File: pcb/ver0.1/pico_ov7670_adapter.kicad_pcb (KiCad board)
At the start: 2 copper layers, 45 x 54 mm, 21 parts, among them J1 GPIO Header, SW1 SW_Push, SW2 SW_Push, U1 CAMERA-OV7670, U2 RASPBERRY_PI_PICO_W

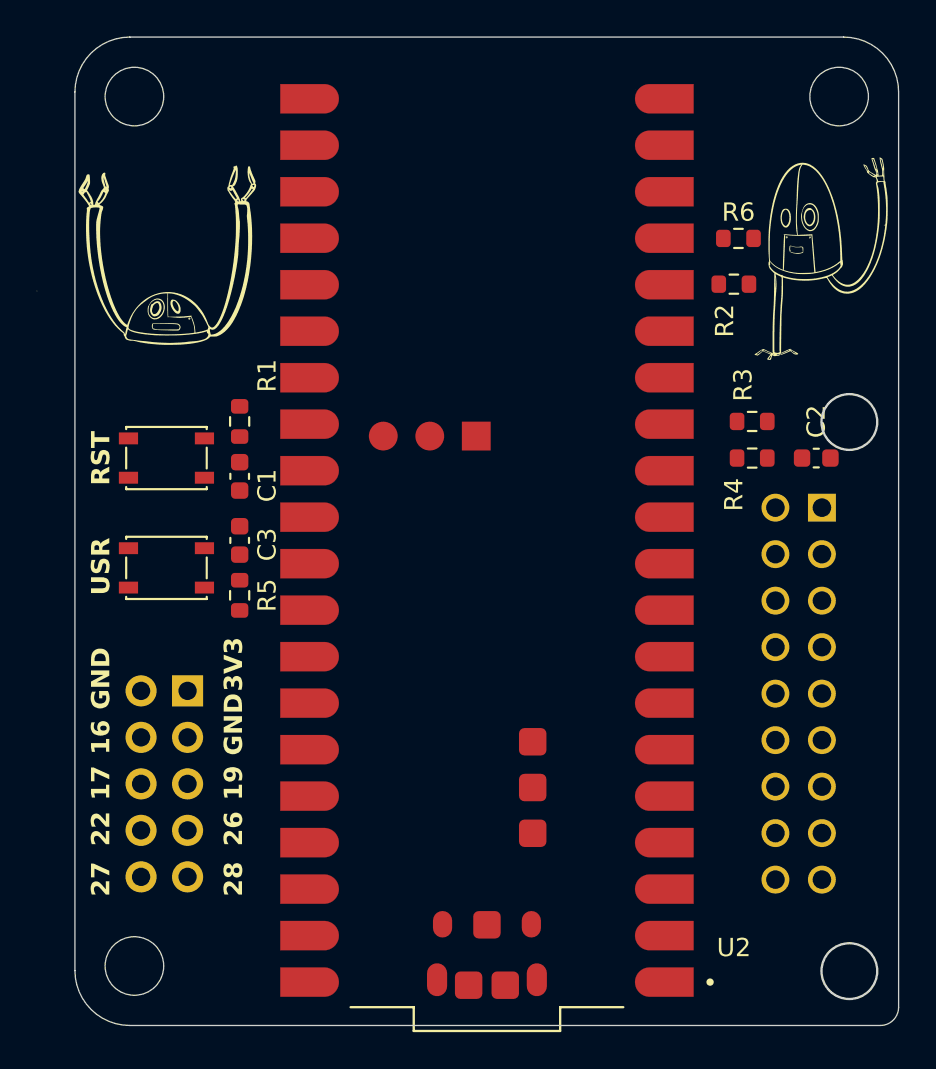
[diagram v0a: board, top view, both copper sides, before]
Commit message: layout updated as per the feedback.
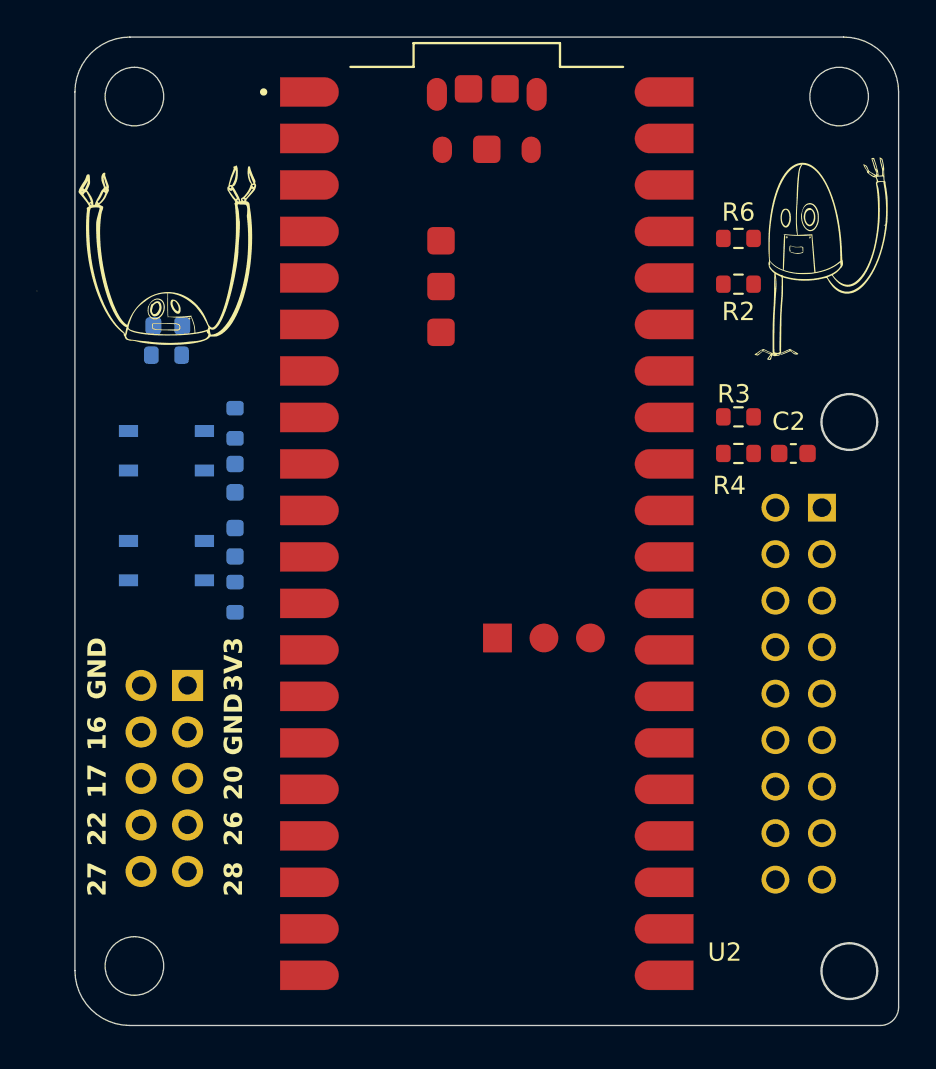
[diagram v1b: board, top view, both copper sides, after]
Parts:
- added D1: USER LED, LED_SMD:LED_0603_1608Metric, B.Cu at (95.1, 81.8)
- added R7: 1K, Resistor_SMD:R_0603_1608Metric, B.Cu at (95.0, 83.4)
- C1, C3, R1, R5, SW1, SW2: moved to B.Cu
- moved G*** 32.6 mm to (128.2, 77.4)
- moved R1 9.60 mm to (98.8, 96.6), turned to 90 degrees
- moved R5 9.40 mm to (98.8, 87.1), turned to 90 degrees
- moved SW2 6.40 mm to (95.0, 88.6)
- moved SW1 5.60 mm to (95.0, 94.6)
- moved C1 3.61 mm to (98.8, 93.6), turned to 90 degrees
- moved C3 3.41 mm to (98.8, 90.1), turned to -90 degrees
- moved C2 1.27 mm to (129.2, 88.8)
- moved G*** 1.01 mm to (113.3, 75.6)
- moved R3 0.79 mm to (126.2, 86.8)
- moved R4 0.79 mm to (126.2, 88.8)
- moved U2 0.37 mm to (112.5, 93.1), turned to 0 degrees
- moved J1 0.30 mm to (96.2, 101.4)
- moved R2 0.25 mm to (126.2, 79.5)
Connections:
- J1 pad 5: /PICO_IO19 -> /PICO_IO20
- U2 pad 25: /PICO_IO19 -> /USER_LED
- U2 pad 26: unconnected-(U2-I2C0_SDA/GP20-Pad26) -> /PICO_IO20
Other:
- board text added: "20"
- board text added: "PICO 2 OV7670 Adapter"
- board text added: "Ver 0.1"
- board text removed: "19"
- board text removed: "PICO 2 OV7670 Adapter 0.1"

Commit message: basic rotuing completed
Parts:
- U2: value RASPBERRY_PI_PICO_W -> MODULE_RASPBERRY_PI_PICO_W
- moved R2 12.1 mm to (125.2, 91.6), turned to 90 degrees
- moved R6 10.9 mm to (125.2, 87.8), turned to 90 degrees
- moved R4 8.37 mm to (129.4, 81.0), turned to -90 degrees
- moved R3 5.86 mm to (127.4, 81.0), turned to -90 degrees
- moved R1 3.35 mm to (98.8, 93.2), turned to -90 degrees
- moved C1 2.65 mm to (98.8, 96.2), turned to -90 degrees
- moved C2 1.57 mm to (128.0, 87.8), turned to 90 degrees
- moved H2 1.00 mm to (93.2, 70.2)
- moved H3 1.00 mm to (131.8, 70.2)
- moved G*** 0.72 mm to (113.4, 76.3)
- moved G*** 0.63 mm to (128.0, 78.0)
- moved G*** 0.35 mm to (129.8, 79.0)
- moved SW1 0.15 mm to (95.0, 94.8)
- moved D1 0.08 mm to (95.0, 81.8)
- turned R5 to -90 degrees
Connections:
- net OV_PCLK_PICO_IO9 renamed OV_PCLK_PICO_IO4
- net OV_XCLK_PICO_IO8 renamed OV_XCLK_PICO_IO5
- J1 pad 10: /PICO_IO27 -> /PICO_IO16
- J1 pad 4: /PICO_IO16 -> /PICO_IO22
- J1 pad 5: /PICO_IO20 -> /PICO_IO21
- J1 pad 6: /PICO_IO17 -> /PICO_IO20
- J1 pad 7: /PICO_IO26 -> /PICO_IO19
- J1 pad 8: /PICO_IO22 -> /PICO_IO18
- J1 pad 9: /PICO_IO28 -> /PICO_IO17
- R2 pad 2: Net-(U2-UART0_TX/I2C0_SDA/SPI1_RX/GP12) -> Net-(U2-UART1_RX/I2C0_SCL/SPI0_CSN/GP5)
- R3 pad 2: OV_SCL_PICO_IO13_SCL -> OV_SCL_PICO_IO1_SCL
- R4 pad 2: OV_SDA_PICO_IO12_SDA -> OV_SDA_PICO_IO0_SDA
- R6 pad 2: Net-(U2-UART0_RX/I2C0_SCL/SPI1_CSN/GP13) -> Net-(U2-UART1_TX/I2C0_SDA/SPI0_RX/GP4)
- U1 pad 11: OV_SDA_PICO_IO12_SDA -> OV_SDA_PICO_IO0_SDA
- U1 pad 12: OV_HREF_PICO_IO11 -> OV_HREF_PICO_IO3
- U1 pad 14: OV_D6_PICO_IO6 -> OV_D6_PICO_IO7
- U1 pad 15: OV_D4_PICO_IO4 -> OV_D4_PICO_IO9
- U1 pad 16: OV_D2_PICO_IO2 -> OV_D2_PICO_IO12
- U1 pad 17: OV_D0_PICO_IO0 -> OV_D0_PICO_IO14
- U1 pad 2: OV_D1_PICO_IO1 -> OV_D1_PICO_IO13
- U1 pad 3: OV_D3_PICO_IO3 -> OV_D3_PICO_IO10
- U1 pad 4: OV_D5_PICO_IO5 -> OV_D5_PICO_IO8
- U1 pad 5: OV_D7_PICO_IO7 -> OV_D7_PICO_IO6
- U1 pad 7: OV_VSYNC_PICO_IO10 -> OV_VSYNC_PICO_IO2
- U1 pad 8: OV_SCL_PICO_IO13_SCL -> OV_SCL_PICO_IO1_SCL
- U2 pad 1: OV_D0_PICO_IO0 -> OV_SDA_PICO_IO0_SDA
- U2 pad 10: OV_D7_PICO_IO7 -> OV_D6_PICO_IO7
- U2 pad 11: OV_SDA_PICO_IO12_SDA -> OV_D5_PICO_IO8
- U2 pad 12: OV_SCL_PICO_IO13_SCL -> OV_D4_PICO_IO9
- U2 pad 14: OV_HREF_PICO_IO11 -> OV_D3_PICO_IO10
- U2 pad 15: OV_VSYNC_PICO_IO10 -> OV_D2_PICO_IO12
- U2 pad 16: Net-(U2-UART0_TX/I2C0_SDA/SPI1_RX/GP12) -> OV_D1_PICO_IO13
- U2 pad 17: Net-(U2-UART0_RX/I2C0_SCL/SPI1_CSN/GP13) -> OV_D0_PICO_IO14
- U2 pad 2: OV_D1_PICO_IO1 -> OV_SCL_PICO_IO1_SCL
- U2 pad 24: /USER_Button -> /PICO_IO18
- U2 pad 25: /USER_LED -> /PICO_IO19
- U2 pad 27: unconnected-(U2-12C0_SCL/GP21-Pad27) -> /PICO_IO21
- U2 pad 31: /PICO_IO26 -> /USER_Button
- U2 pad 32: /PICO_IO27 -> unconnected-(U2-I2C1_SCL/ADC1/GP27-Pad32)
- U2 pad 34: /PICO_IO28 -> /USER_LED
- U2 pad 4: OV_D2_PICO_IO2 -> OV_VSYNC_PICO_IO2
- U2 pad 5: OV_D3_PICO_IO3 -> OV_HREF_PICO_IO3
- U2 pad 6: OV_D4_PICO_IO4 -> Net-(U2-UART1_TX/I2C0_SDA/SPI0_RX/GP4)
- U2 pad 7: OV_D5_PICO_IO5 -> Net-(U2-UART1_RX/I2C0_SCL/SPI0_CSN/GP5)
- U2 pad 9: OV_D6_PICO_IO6 -> OV_D7_PICO_IO6
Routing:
- net +3V3: track 0.00 -> 87.3 mm, vias 0 -> 5
- net OV_SDA_PICO_IO0_SDA: track 0.00 -> 59.8 mm
- net OV_SCL_PICO_IO1_SCL: track 0.00 -> 45.4 mm
- net OV_VSYNC_PICO_IO2: track 0.00 -> 42.3 mm
- net /PICO_IO22: track 0.00 -> 40.2 mm
- net OV_HREF_PICO_IO3: track 0.00 -> 38.6 mm
- net OV_D7_PICO_IO6: track 0.00 -> 35.6 mm
- net /PICO_RESET: track 0.00 -> 35.4 mm, vias 0 -> 1
- net OV_D5_PICO_IO8: track 0.00 -> 33.5 mm
- net /USER_Button: track 0.00 -> 32.6 mm, vias 0 -> 1
- net /USER_LED: track 0.00 -> 32.3 mm, vias 0 -> 1
- net /PICO_IO16: track 0.00 -> 32.2 mm
- net OV_D6_PICO_IO7: track 0.00 -> 31.6 mm
- net /PICO_IO20: track 0.00 -> 31.6 mm
- net /PICO_IO18: track 0.00 -> 30.3 mm
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- added copper zone on B.Cu, net GND
- added copper zone on F.Cu, net GND
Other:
- board size 45 x 54 mm -> 45 x 53 mm
- board text added: "18"
- board text added: "19"
- board text added: "21"
- board text removed: "26"
- board text removed: "27"
- board text removed: "28"

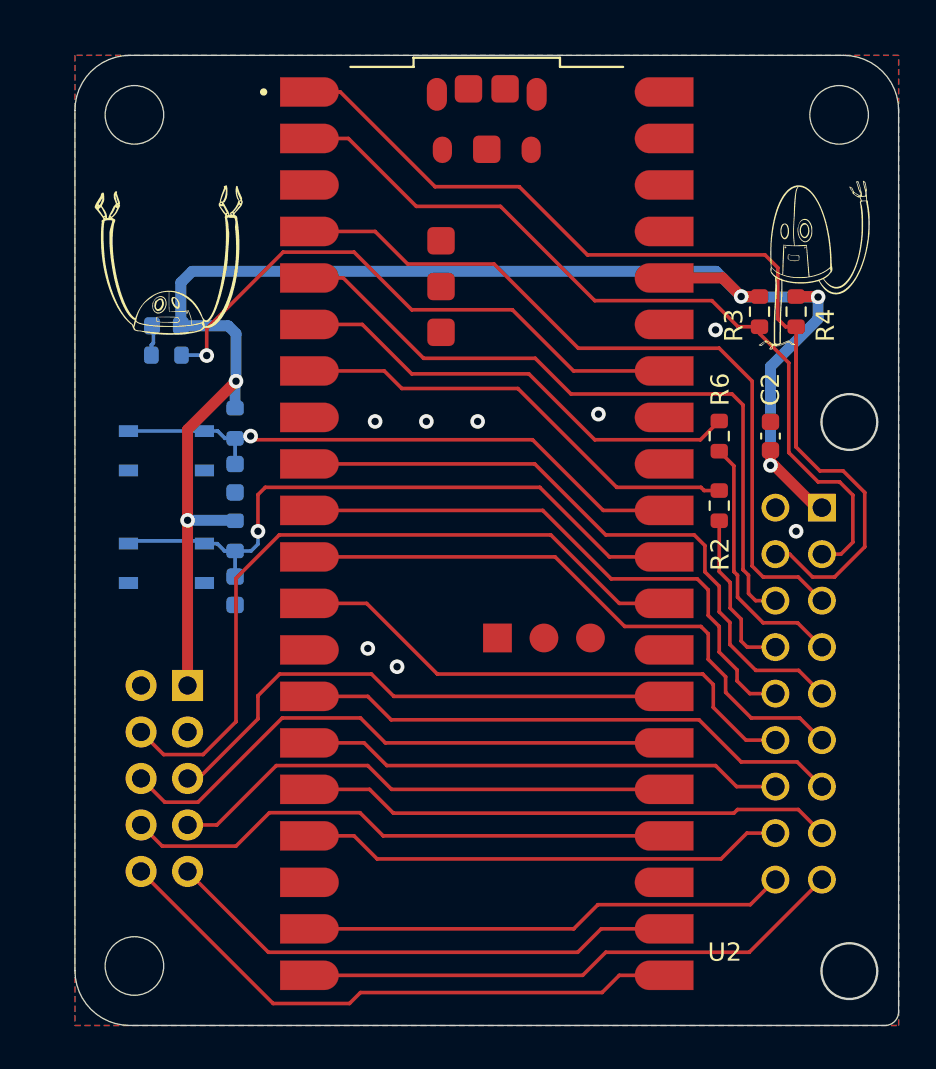
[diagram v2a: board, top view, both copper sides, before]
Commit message: GPIO header change updated
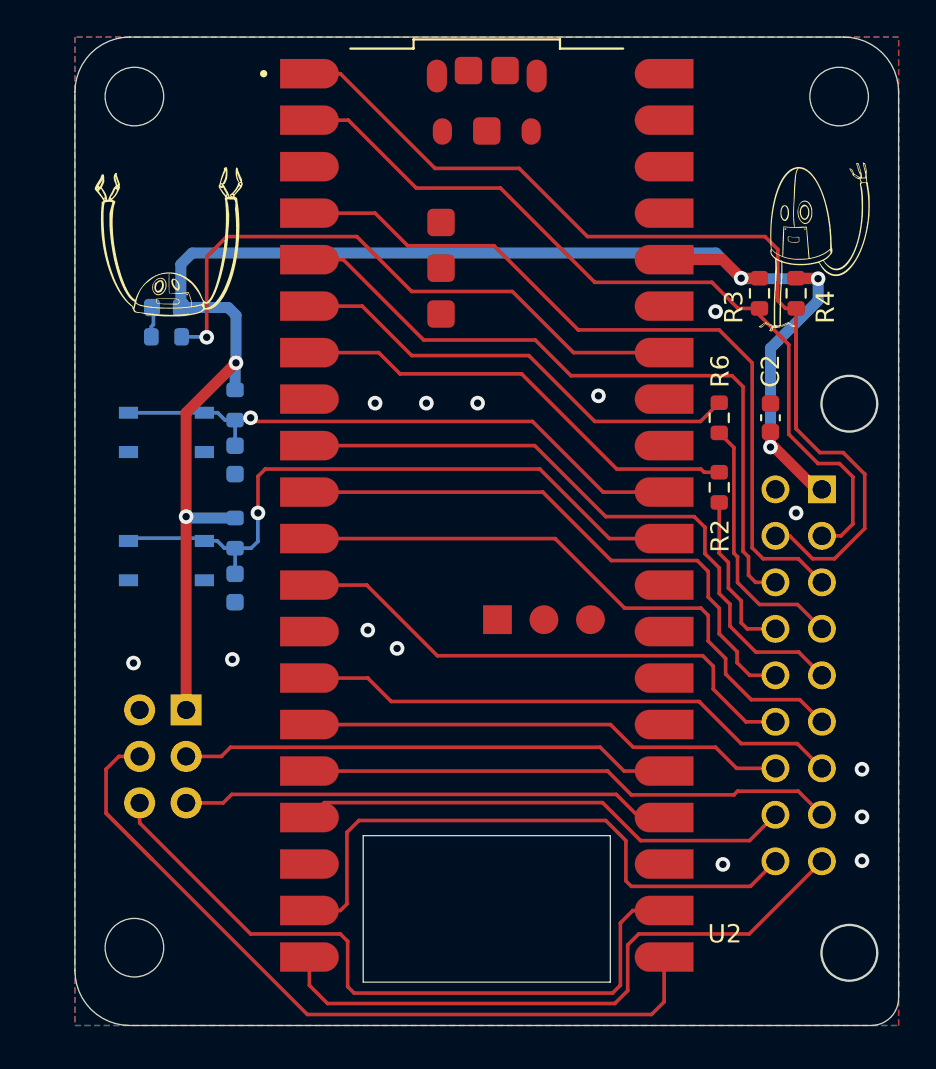
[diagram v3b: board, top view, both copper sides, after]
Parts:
- J1: footprint Connector_PinHeader_2.54mm:PinHeader_2x05_P2.54mm_Vertical -> Connector_PinHeader_2.54mm:PinHeader_2x03_P2.54mm_Vertical
- moved J1 1.34 mm to (96.1, 102.8)
- moved C2 1.00 mm to (128.0, 86.8)
- moved C3 1.00 mm to (98.8, 89.1)
- moved D1 1.00 mm to (95.0, 80.8)
- moved G*** 1.00 mm to (95.5, 78.5)
- moved G*** 1.00 mm to (129.8, 78.0)
- moved G*** 1.00 mm to (113.4, 75.3)
- moved G*** 1.00 mm to (128.0, 77.0)
- moved H1 1.00 mm to (93.2, 115.8)
- moved H2 1.00 mm to (93.2, 69.2)
- moved H3 1.00 mm to (131.8, 69.2)
- moved R2 1.00 mm to (125.2, 90.6)
- moved R3 1.00 mm to (127.4, 80.0)
- moved R4 1.00 mm to (129.4, 80.0)
- moved R5 1.00 mm to (98.8, 86.1)
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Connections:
- J1 pad 3: GND -> /PICO_IO19
- J1 pad 4: /PICO_IO22 -> /PICO_IO16
- J1 pad 5: /PICO_IO21 -> /PICO_IO18
- J1 pad 6: /PICO_IO20 -> /PICO_IO17
- U2 pad 26: /PICO_IO20 -> unconnected-(U2-I2C0_SDA/GP20-Pad26)
- U2 pad 27: /PICO_IO21 -> unconnected-(U2-12C0_SCL/GP21-Pad27)
- U2 pad 29: /PICO_IO22 -> unconnected-(U2-GP22-Pad29)
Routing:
- net /PICO_IO22: track 40.2 -> 0.00 mm
- net /PICO_IO20: track 31.6 -> 0.00 mm
- net /PICO_IO21: track 29.7 -> 0.00 mm
- net /PICO_IO16: track 32.2 -> 45.8 mm
- net /PICO_IO17: track 28.4 -> 38.9 mm
- net OV_PWDWN_PICO_IO15: track 26.6 -> 33.1 mm
- net OV_RST_PICO_IO14: track 30.2 -> 34.6 mm
- net /PICO_IO18: track 30.3 -> 26.8 mm
- net +3V3: track 87.3 -> 89.8 mm
- net /USER_LED: track 32.3 -> 33.9 mm
- net /PICO_IO19: track 27.9 -> 26.8 mm
- net /PICO_RESET: track 35.4 -> 36.3 mm
- net OV_D0_PICO_IO14: track 26.6 -> 27.2 mm
- net GND: vias 8 -> 14
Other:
- board size 45 x 53 mm -> 45 x 54 mm
- board text added: "16_T"
- board text added: "17_R"
- board text removed: "16"
- board text removed: "17"
- board text removed: "20"
- board text removed: "21"
- board text removed: "22"

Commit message: gerber files added
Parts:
- added FID1: Fiducial, Fiducial:Fiducial_0.5mm_Mask1mm, F.Cu at (129.0, 118.6)
- added FID2: Fiducial, Fiducial:Fiducial_0.5mm_Mask1mm, F.Cu at (97.2, 118.6)
- added FID3: Fiducial, Fiducial:Fiducial_0.5mm_Mask1mm, F.Cu at (97.2, 67.2)
- U2: value MODULE_RASPBERRY_PI_PICO_W -> RASPBERRY_PI_PICO_W
- moved H1 1.00 mm to (93.2, 116.8)
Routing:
- net GND: vias 14 -> 66
